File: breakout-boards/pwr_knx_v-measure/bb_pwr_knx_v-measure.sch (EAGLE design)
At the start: 48 parts, among them IC100 BD9G101, T1 BC856, T2 BCP52, T3 BC847

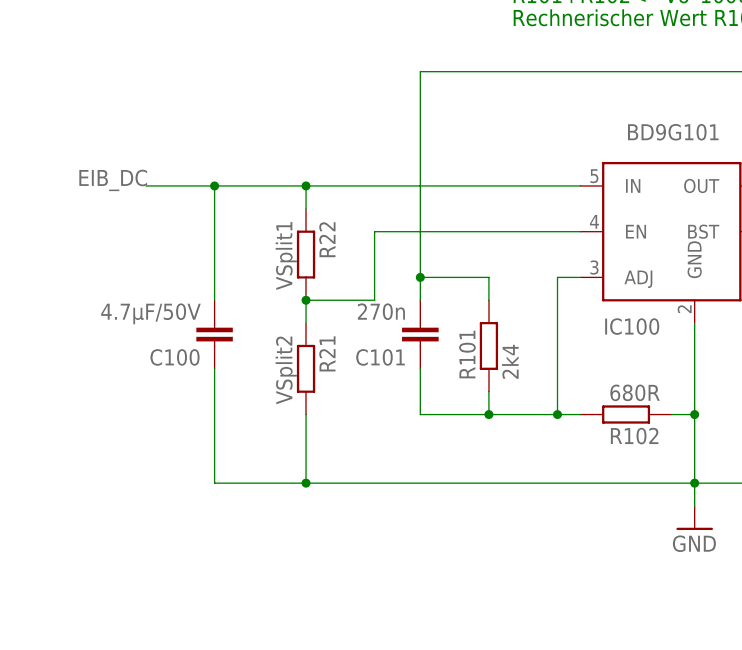
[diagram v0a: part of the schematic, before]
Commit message: [BB_Pwr+KNX] - removed v-split at buck's enable pin
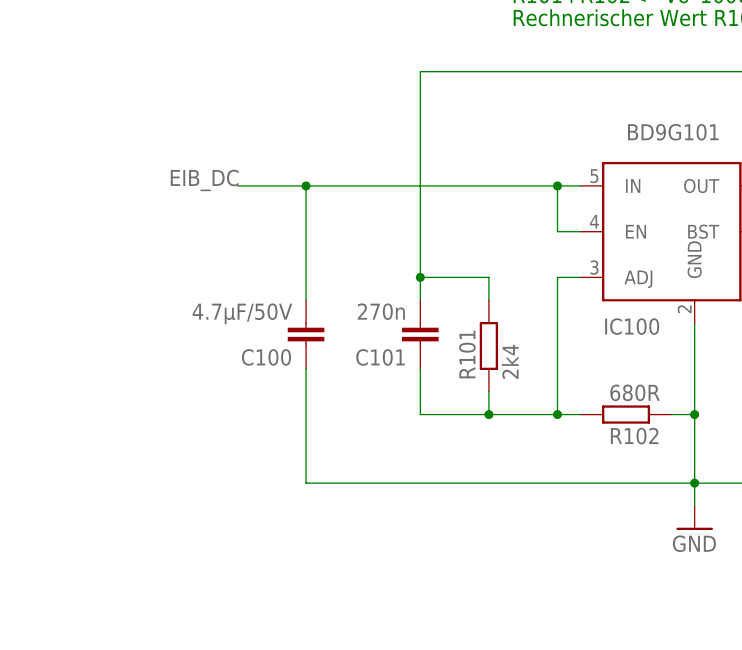
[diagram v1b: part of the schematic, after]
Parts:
- removed R21: VSplit2, rcl:R-EU_R0805
- removed R22: VSplit1, rcl:R-EU_R0805
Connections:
- removed net N$5: IC100.EN, R21.1, R22.2
- net EIB_DC: now also IC100.EN; no longer R22.1
- net GND: no longer R21.2
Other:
- moved on the sheet: C100
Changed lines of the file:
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@@
 <attribute name="REICHELT" value="1N 4148 SMD"/>
 </part>
-<part name="R21" library="rcl" library_urn="urn:adsk.eagle:library:334" deviceset="R-EU_" device="R0805" package3d_urn="urn:adsk.eagle:package:23553/2" value="VSplit2"/>
-<part name="R22" library="rcl" library_urn="urn:adsk.eagle:library:334" deviceset="R-EU_" device="R0805" package3d_urn="urn:adsk.eagle:package:23553/2" value="VSplit1"/>
 <part name="U$1" library="Connector_for_Selfbus-Projects" deviceset="WAGO-243-211" device=""/>
 <part name="R25" library="rcl" library_urn="urn:adsk.eagle:library:334" deviceset="R-EU_" device="R2512" package3d_urn="urn:adsk.eagle:package:23545/2" value="24R  1210/0.5W">
@@
 <attribute name="VALUE" x="125.857" y="259.588" size="1.778" layer="96" rot="R180"/>
 </instance>
-<instance part="C100" gate="G$1" x="30.48" y="243.84" smashed="yes" rot="R180">
-<attribute name="REICHELT" x="30.48" y="243.84" size="1.778" layer="96" rot="R180" display="off"/>
-<attribute name="NAME" x="28.956" y="243.459" size="1.778" layer="95" rot="R180"/>
-<attribute name="VALUE" x="28.956" y="248.539" size="1.778" layer="96" rot="R180"/>
+<instance part="C100" gate="G$1" x="40.64" y="243.84" smashed="yes" rot="R180">
+<attribute name="REICHELT" x="40.64" y="243.84" size="1.778" layer="96" rot="R180" display="off"/>
+<attribute name="NAME" x="39.116" y="243.459" size="1.778" layer="95" rot="R180"/>
+<attribute name="VALUE" x="39.116" y="248.539" size="1.778" layer="96" rot="R180"/>
 </instance>
 <instance part="C103" gate="G$1" x="134.62" y="248.92" smashed="yes" rot="MR0">
@@
 <attribute name="NAME" x="40.64" y="178.2826" size="1.778" layer="95"/>
 <attribute name="VALUE" x="40.64" y="175.4886" size="1.778" layer="96"/>
-</instance>
-<instance part="R21" gate="G$1" x="40.64" y="241.3" smashed="yes" rot="R270">
-<attribute name="NAME" x="42.1386" y="245.11" size="1.778" layer="95" rot="R270"/>
-<attribute name="VALUE" x="37.338" y="245.11" size="1.778" layer="96" rot="R270"/>
-</instance>
-<instance part="R22" gate="G$1" x="40.64" y="254" smashed="yes" rot="R270">
-<attribute name="NAME" x="42.1386" y="257.81" size="1.778" layer="95" rot="R270"/>
-<attribute name="VALUE" x="37.338" y="257.81" size="1.778" layer="96" rot="R270"/>
 </instance>
 <instance part="U$1" gate="G$1" x="22.86" y="137.16" smashed="yes" rot="MR0">
@@
 <junction x="83.82" y="236.22"/>
 <junction x="83.82" y="228.6"/>
-<pinref part="R21" gate="G$1" pin="2"/>
-<wire x1="40.64" y1="236.22" x2="40.64" y2="228.6" width="0.1524" layer="91"/>
 <pinref part="C100" gate="G$1" pin="1"/>
-<wire x1="30.48" y1="241.3" x2="30.48" y2="228.6" width="0.1524" layer="91"/>
-<wire x1="40.64" y1="228.6" x2="30.48" y2="228.6" width="0.1524" layer="91"/>
-<junction x="40.64" y="228.6"/>
+<wire x1="40.64" y1="241.3" x2="40.64" y2="228.6" width="0.1524" layer="91"/>
 <pinref part="D100" gate="1" pin="A"/>
 <wire x1="106.68" y1="241.3" x2="106.68" y2="238.76" width="0.1524" layer="91"/>
@@
 <segment>
 <pinref part="IC100" gate="G$1" pin="IN"/>
-<wire x1="40.64" y1="261.62" x2="71.12" y2="261.62" width="0.1524" layer="91"/>
-<pinref part="R22" gate="G$1" pin="1"/>
-<wire x1="40.64" y1="259.08" x2="40.64" y2="261.62" width="0.1524" layer="91"/>
+<wire x1="40.64" y1="261.62" x2="68.58" y2="261.62" width="0.1524" layer="91"/>
+<wire x1="68.58" y1="261.62" x2="71.12" y2="261.62" width="0.1524" layer="91"/>
+<wire x1="33.02" y1="261.62" x2="40.64" y2="261.62" width="0.1524" layer="91"/>
 <junction x="40.64" y="261.62"/>
-<wire x1="22.86" y1="261.62" x2="30.48" y2="261.62" width="0.1524" layer="91"/>
-<wire x1="30.48" y1="261.62" x2="40.64" y2="261.62" width="0.1524" layer="91"/>
-<junction x="30.48" y="261.62"/>
 <pinref part="C100" gate="G$1" pin="2"/>
-<wire x1="30.48" y1="248.92" x2="30.48" y2="261.62" width="0.1524" layer="91"/>
-<label x="15.24" y="261.62" size="1.778" layer="95"/>
+<wire x1="40.64" y1="248.92" x2="40.64" y2="261.62" width="0.1524" layer="91"/>
+<label x="25.4" y="261.62" size="1.778" layer="95"/>
+<pinref part="IC100" gate="G$1" pin="EN"/>
+<wire x1="71.12" y1="256.54" x2="68.58" y2="256.54" width="0.1524" layer="91"/>
+<wire x1="68.58" y1="256.54" x2="68.58" y2="261.62" width="0.1524" layer="91"/>
+<junction x="68.58" y="261.62"/>
 </segment>
 </net>
@@
 </segment>
 </net>
-<net name="N$5" class="0">
-<segment>
-<pinref part="IC100" gate="G$1" pin="EN"/>
-<pinref part="R22" gate="G$1" pin="2"/>
-<pinref part="R21" gate="G$1" pin="1"/>
-<wire x1="40.64" y1="246.38" x2="40.64" y2="248.92" width="0.1524" layer="91"/>
-<junction x="40.64" y="248.92"/>
-<wire x1="40.64" y1="248.92" x2="48.26" y2="248.92" width="0.1524" layer="91"/>
-<wire x1="48.26" y1="248.92" x2="48.26" y2="256.54" width="0.1524" layer="91"/>
-<wire x1="48.26" y1="256.54" x2="71.12" y2="256.54" width="0.1524" layer="91"/>
-</segment>
-</net>

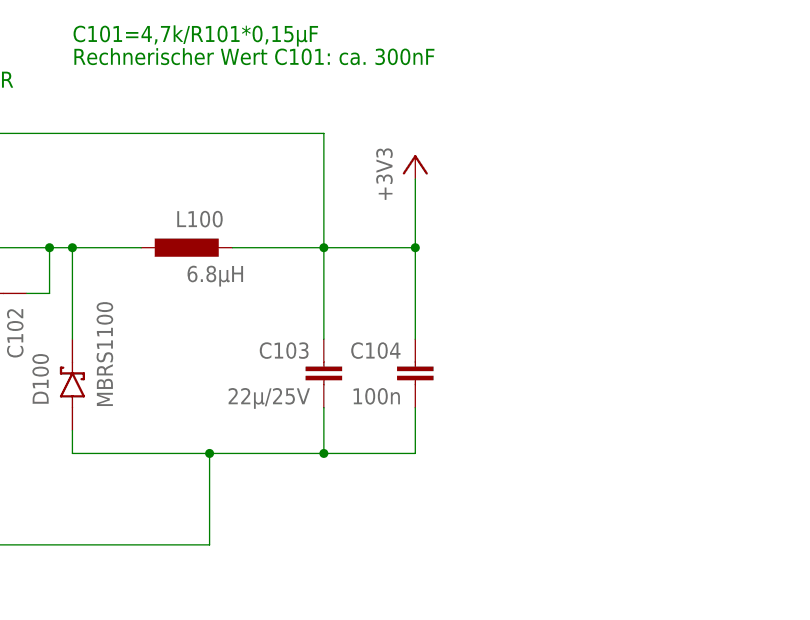
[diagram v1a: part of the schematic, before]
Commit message: [BB_Pwr+KNX] removed attributes, switched to 2x47uF mlccs
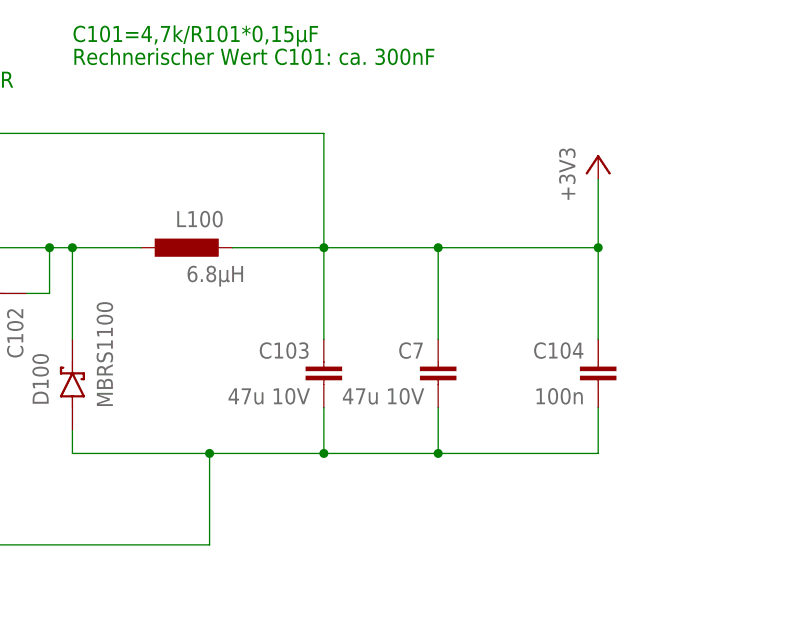
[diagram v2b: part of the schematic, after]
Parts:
- added C7: 47u 10V, rcl:C-EUC0805
- C1: REICHELT VF 100/35 K-D8 -> (none)
- C10, C104, C2: REICHELT X7R-G0805 100N -> (none)
- C100: REICHELT X7R-G1206 4,7/50 -> (none)
- C101: REICHELT Y5R-G0603 220N -> (none)
- C102: REICHELT X7R-G0805 15N -> (none)
- C103: value 22µ/25V -> 47u 10V; device rcl:C-EUC1206 -> rcl:C-EUC0805; REICHELT X5R-G0805 22/6 -> (none)
- C3, C4, C6: REICHELT X7R-G0805 10N -> (none)
- C5: REICHELT NPO-G0805 100P -> (none)
- D100: REICHELT MBRS 1100 SMD -> (none)
- D2, D3, D4, D5: REICHELT 1N 4148 SMD -> (none)
- D6: REICHELT SMD ZF 7,5 -> (none)
- D7: REICHELT SMD ZF 3,6 -> (none)
- L1: REICHELT L-11P 150M -> (none)
- R1, R3: REICHELT SMD-0805 1,00K -> (none)
- R10, R13, R7: REICHELT SMD-0805 10,0K -> (none)
- R101: REICHELT SMD 1/4W 2,4K -> (none)
- R102: REICHELT SMD-0805 680 -> (none)
- R11, R5: REICHELT SMD-0805 100K -> (none)
- R12: REICHELT SMD 1/4W 91K -> (none)
- R2, R25: REICHELT SMD-0805 5,60 -> (none)
- R4: REICHELT SMD-0805 2,20K -> (none)
- R6: REICHELT SMD-0805 5,60K -> (none)
- R8: REICHELT SMD-0805 82,0K -> (none)
- R9: REICHELT SMD-0805 47,0K -> (none)
- T1: REICHELT BC 856B SMD -> (none)
- T2: REICHELT BCP 52-16 SMD -> (none)
- T3: REICHELT BC 847C SMD -> (none)
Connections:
- net +3V3: now also C7.1
- net GND: now also C7.2
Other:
- moved on the sheet: C104

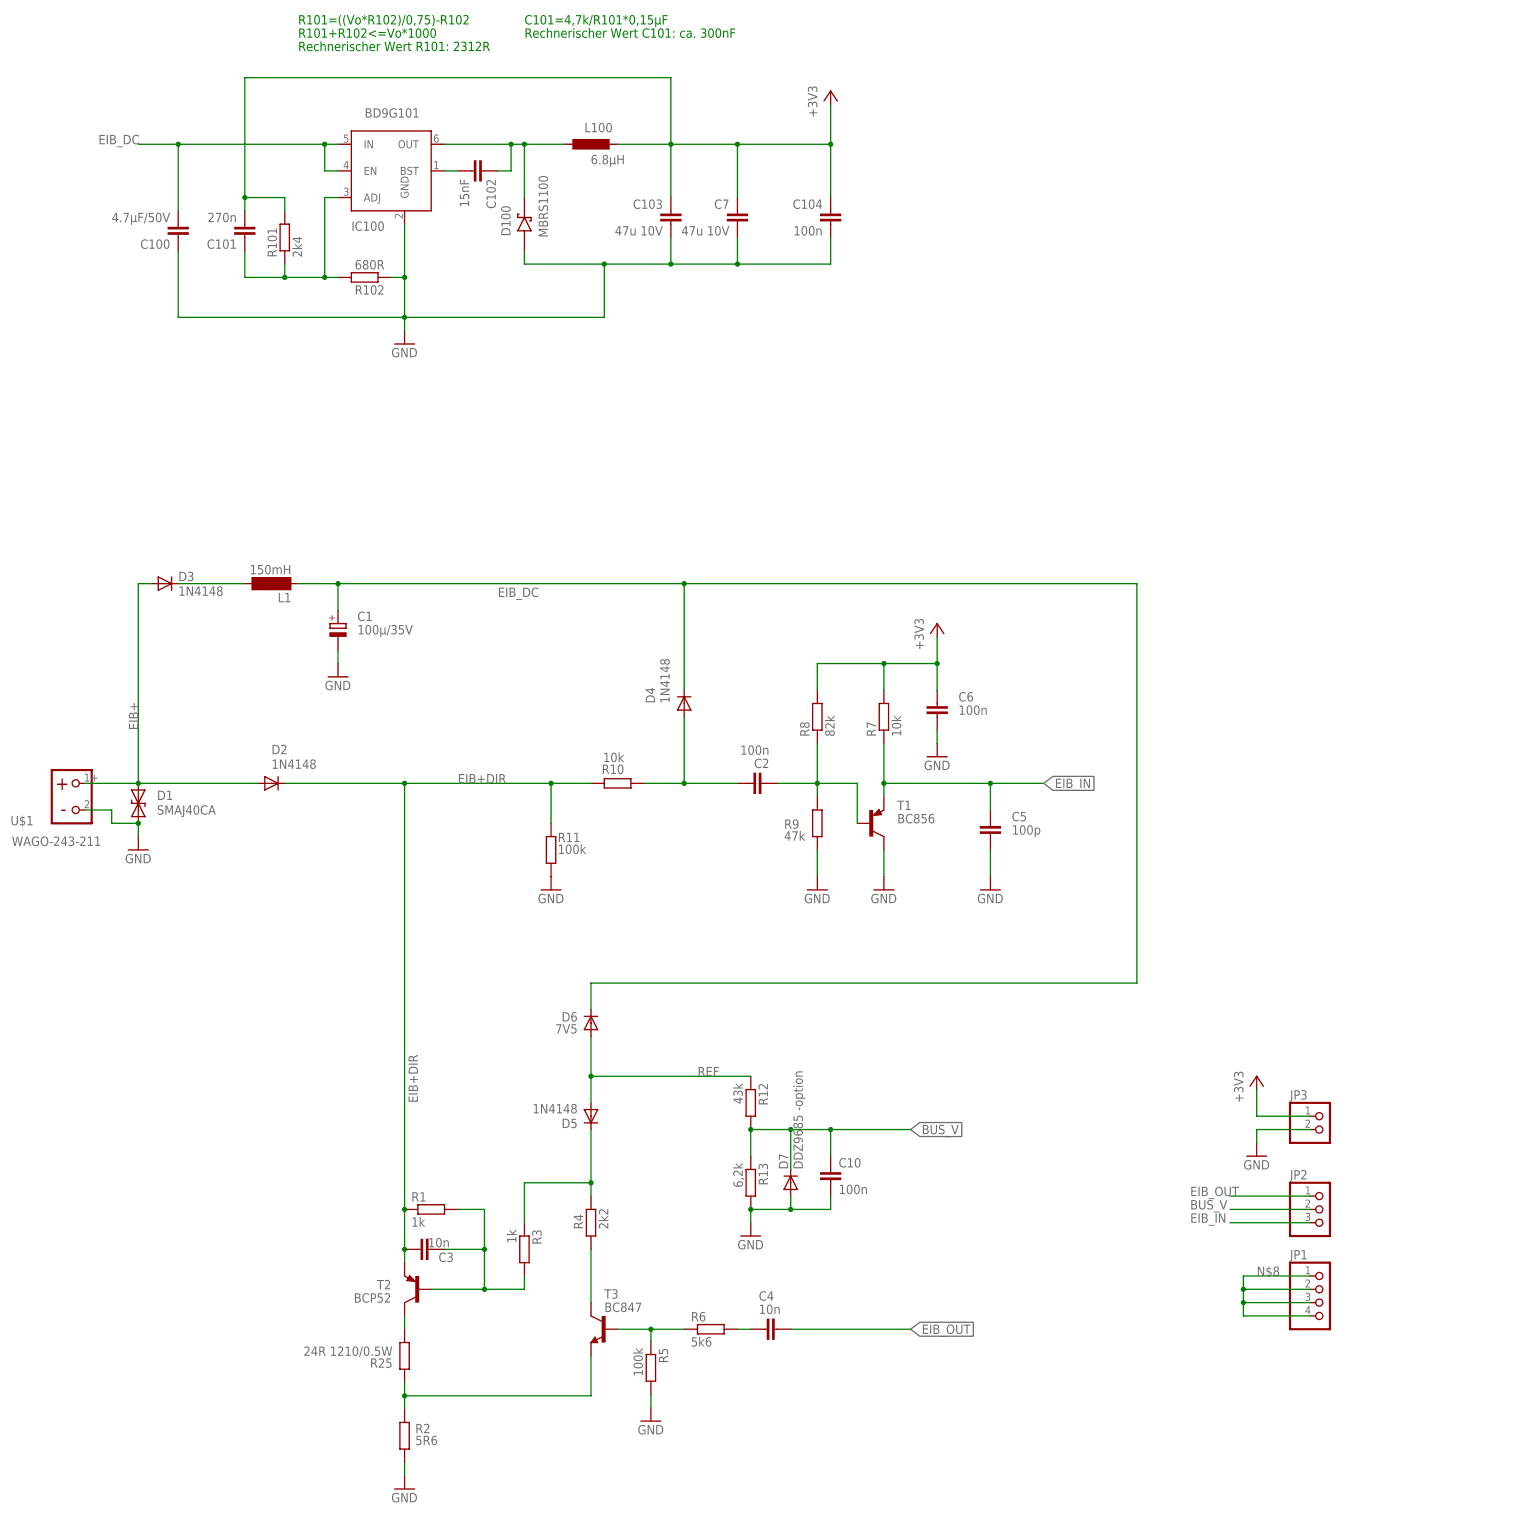
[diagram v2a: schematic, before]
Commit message: [BB_Pwr+KNX] - changed values to standard values
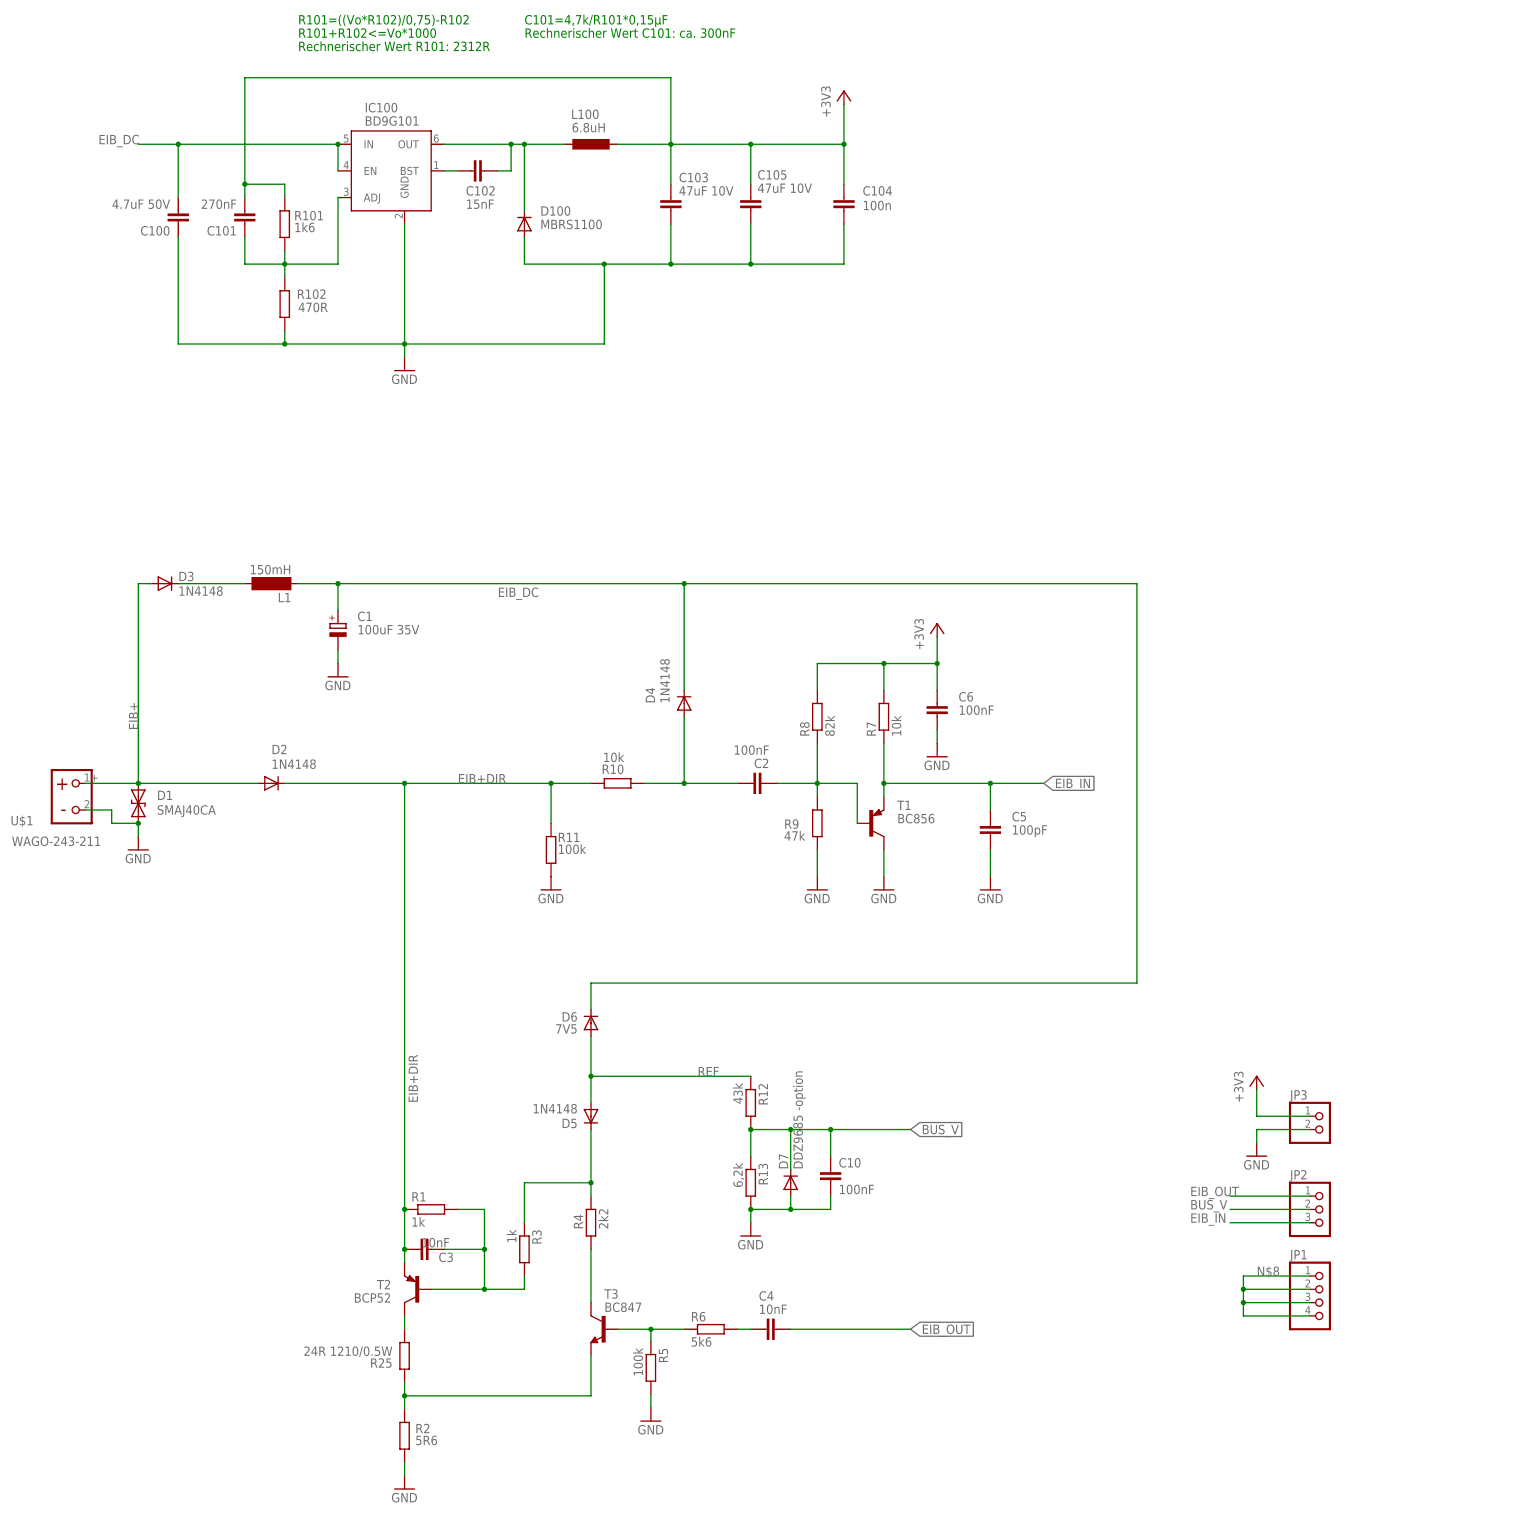
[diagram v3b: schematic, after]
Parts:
- removed C7: 47u 10V, rcl:C-EUC0805
- added C105: 47uF 10V, rcl:C-EUC0805
- C1: value 100µ/35V -> 100uF 35V
- C10, C2, C6: value 100n -> 100nF
- C100: value 4.7µF/50V -> 4.7uF 50V
- C101: value 270n -> 270nF
- C103: value 47u 10V -> 47uF 10V
- C3, C4: value 10n -> 10nF
- C5: value 100p -> 100pF
- D100: device bt_diode:SCHOTTKY-DIODE-MBR130LSFT1 -> microbuilder:DIODESOD-123
- L100: value 6.8µH -> 6.8uH; REICHELT L-1616FPS 6,8µ -> (none)
- R101: value 2k4 -> 1k6
- R102: value 680R -> 470R
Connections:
- net +3V3: now also C105.1; no longer C7.1
- net GND: now also C105.2; no longer C7.2
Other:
- moved on the sheet: C100, C101, C103, C104, R101, R102
